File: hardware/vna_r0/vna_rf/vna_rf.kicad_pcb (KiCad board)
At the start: 4 copper layers, 78 x 49 mm, 258 parts, among them J301 RF_Shield_Two_Pieces, J302 RF_Shield_Two_Pieces, J401 CONN_02X10, J402 RF_Shield_Two_Pieces, U201 LMX2594, U202 LTC2630, U203 ADRF5040, U204 LTC2054CS5, U205 MAAM-011100, U301 NC7WZU04, U302 PE42521, U303 MASW-008322-TR1000, U304 PE42521, U401 CONN_SMA_2GND, U402 CONN_SMA_2GND, U403 CONN_SMA, U404 CONN_SMA, U405 CONN_SMA, U406 CONN_SMA_2GND

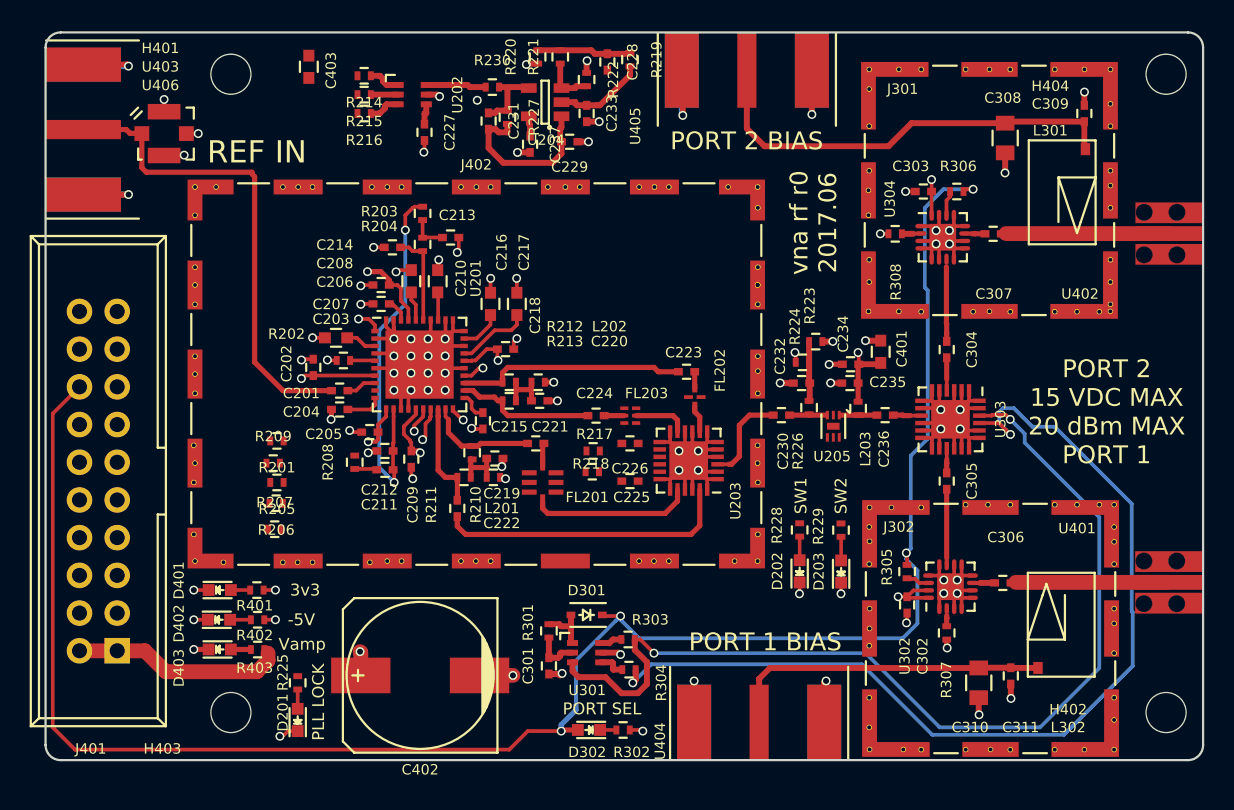
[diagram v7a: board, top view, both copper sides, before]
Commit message: finished vna rf r0 layout
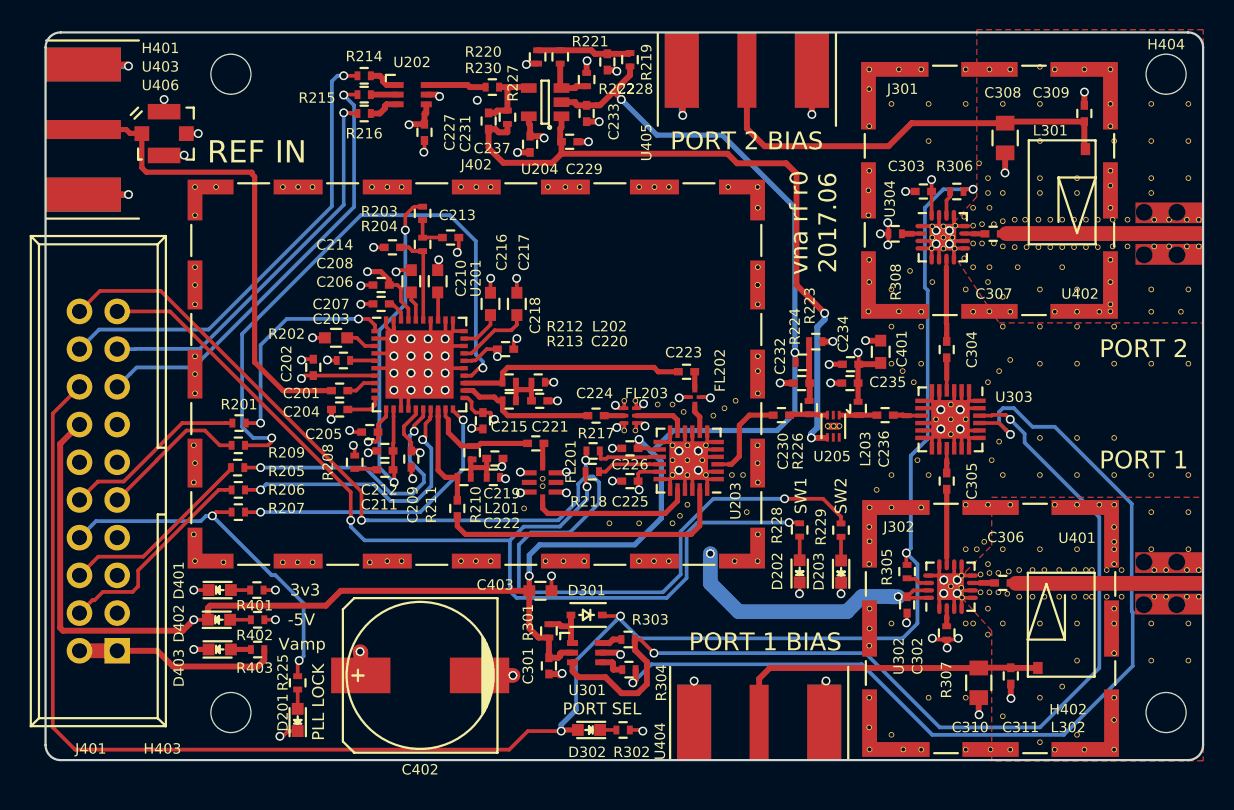
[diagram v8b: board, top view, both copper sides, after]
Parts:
- added REF**: VIA_OSH4LAYER_MIN, vna_footprints:VIA_OSH4LAYER_MIN, F.Cu at (207.8, 107.2)
- added REF**: VIA_OSH4LAYER_MIN, vna_footprints:VIA_OSH4LAYER_MIN, F.Cu at (216.8, 100.2)
- added REF**: VIA_OSH4LAYER_MIN, vna_footprints:VIA_OSH4LAYER_MIN, F.Cu at (252.0, 94.0)
- added REF**: VIA_OSH4LAYER_MIN, vna_footprints:VIA_OSH4LAYER_MIN, F.Cu at (250.0, 94.0)
- added REF**: VIA_OSH4LAYER_MIN, vna_footprints:VIA_OSH4LAYER_MIN, F.Cu at (244.0, 91.0)
- added REF**: VIA_OSH4LAYER_MIN, vna_footprints:VIA_OSH4LAYER_MIN, F.Cu at (241.0, 91.0)
- added REF**: VIA_OSH4LAYER_MIN, vna_footprints:VIA_OSH4LAYER_MIN, F.Cu at (240.0, 121.2)
- added REF**: VIA_OSH4LAYER_MIN, vna_footprints:VIA_OSH4LAYER_MIN, F.Cu at (242.5, 123.0)
- added REF**: VIA_OSH4LAYER_MIN, vna_footprints:VIA_OSH4LAYER_MIN, F.Cu at (245.0, 122.5)
- added REF**: VIA_OSH4LAYER_MIN, vna_footprints:VIA_OSH4LAYER_MIN, F.Cu at (242.5, 120.0)
- added REF**: VIA_OSH4LAYER_MIN, vna_footprints:VIA_OSH4LAYER_MIN, F.Cu at (244.0, 119.2)
- added REF**: VIA_OSH4LAYER_MIN, vna_footprints:VIA_OSH4LAYER_MIN, F.Cu at (245.0, 117.5)
- added REF**: VIA_OSH4LAYER_MIN, vna_footprints:VIA_OSH4LAYER_MIN, F.Cu at (217.8, 100.2)
- added REF**: VIA_OSH4LAYER_MIN, vna_footprints:VIA_OSH4LAYER_MIN, F.Cu at (250.0, 117.5)
- added REF**: VIA_OSH4LAYER_MIN, vna_footprints:VIA_OSH4LAYER_MIN, F.Cu at (252.5, 117.5)
- added REF**: VIA_OSH4LAYER_MIN, vna_footprints:VIA_OSH4LAYER_MIN, F.Cu at (252.5, 115.0)
- added REF**: VIA_OSH4LAYER_MIN, vna_footprints:VIA_OSH4LAYER_MIN, F.Cu at (250.0, 115.0)
- added REF**: VIA_OSH4LAYER_MIN, vna_footprints:VIA_OSH4LAYER_MIN, F.Cu at (245.0, 115.0)
- added REF**: VIA_OSH4LAYER_MIN, vna_footprints:VIA_OSH4LAYER_MIN, F.Cu at (242.5, 115.0)
- added REF**: VIA_OSH4LAYER_MIN, vna_footprints:VIA_OSH4LAYER_MIN, F.Cu at (240.0, 115.0)
- added REF**: VIA_OSH4LAYER_MIN, vna_footprints:VIA_OSH4LAYER_MIN, F.Cu at (240.0, 110.0)
- added REF**: VIA_OSH4LAYER_MIN, vna_footprints:VIA_OSH4LAYER_MIN, F.Cu at (242.5, 110.0)
- added REF**: VIA_OSH4LAYER_MIN, vna_footprints:VIA_OSH4LAYER_MIN, F.Cu at (245.0, 110.0)
- added REF**: VIA_OSH4LAYER_MIN, vna_footprints:VIA_OSH4LAYER_MIN, F.Cu at (218.5, 100.8)
- added REF**: VIA_OSH4LAYER_MIN, vna_footprints:VIA_OSH4LAYER_MIN, F.Cu at (247.5, 110.0)
- added REF**: VIA_OSH4LAYER_MIN, vna_footprints:VIA_OSH4LAYER_MIN, F.Cu at (250.0, 110.0)
- added REF**: VIA_OSH4LAYER_MIN, vna_footprints:VIA_OSH4LAYER_MIN, F.Cu at (252.5, 110.0)
- added REF**: VIA_OSH4LAYER_MIN, vna_footprints:VIA_OSH4LAYER_MIN, F.Cu at (250.0, 107.5)
- added REF**: VIA_OSH4LAYER_MIN, vna_footprints:VIA_OSH4LAYER_MIN, F.Cu at (252.5, 107.5)
- added REF**: VIA_OSH4LAYER_MIN, vna_footprints:VIA_OSH4LAYER_MIN, F.Cu at (242.5, 92.5)
- added REF**: VIA_OSH4LAYER_MIN, vna_footprints:VIA_OSH4LAYER_MIN, F.Cu at (245.0, 92.5)
- added REF**: VIA_OSH4LAYER_MIN, vna_footprints:VIA_OSH4LAYER_MIN, F.Cu at (250.0, 92.5)
- added REF**: VIA_OSH4LAYER_MIN, vna_footprints:VIA_OSH4LAYER_MIN, F.Cu at (252.5, 92.5)
- added REF**: VIA_OSH4LAYER_MIN, vna_footprints:VIA_OSH4LAYER_MIN, F.Cu at (252.5, 85.0)
- added REF**: VIA_OSH4LAYER_MIN, vna_footprints:VIA_OSH4LAYER_MIN, F.Cu at (217.8, 108.2)
- added REF**: VIA_OSH4LAYER_MIN, vna_footprints:VIA_OSH4LAYER_MIN, F.Cu at (250.0, 85.0)
- added REF**: VIA_OSH4LAYER_MIN, vna_footprints:VIA_OSH4LAYER_MIN, F.Cu at (245.0, 85.0)
- added REF**: VIA_OSH4LAYER_MIN, vna_footprints:VIA_OSH4LAYER_MIN, F.Cu at (242.5, 85.0)
- added REF**: VIA_OSH4LAYER_MIN, vna_footprints:VIA_OSH4LAYER_MIN, F.Cu at (242.5, 77.5)
- added REF**: VIA_OSH4LAYER_MIN, vna_footprints:VIA_OSH4LAYER_MIN, F.Cu at (252.5, 80.0)
- added REF**: VIA_OSH4LAYER_MIN, vna_footprints:VIA_OSH4LAYER_MIN, F.Cu at (250.0, 80.0)
- added REF**: VIA_OSH4LAYER_MIN, vna_footprints:VIA_OSH4LAYER_MIN, F.Cu at (240.0, 80.0)
- added REF**: VIA_OSH4LAYER_MIN, vna_footprints:VIA_OSH4LAYER_MIN, F.Cu at (242.5, 80.0)
- added REF**: VIA_OSH4LAYER_MIN, vna_footprints:VIA_OSH4LAYER_MIN, F.Cu at (247.5, 82.5)
- added REF**: VIA_OSH4LAYER_MIN, vna_footprints:VIA_OSH4LAYER_MIN, F.Cu at (252.5, 82.5)
- added REF**: VIA_OSH4LAYER_MIN, vna_footprints:VIA_OSH4LAYER_MIN, F.Cu at (218.2, 107.8)
- added REF**: VIA_OSH4LAYER_MIN, vna_footprints:VIA_OSH4LAYER_MIN, F.Cu at (242.5, 82.5)
- added REF**: VIA_OSH4LAYER_MIN, vna_footprints:VIA_OSH4LAYER_MIN, F.Cu at (250.0, 82.5)
- added REF**: VIA_OSH4LAYER_MIN, vna_footprints:VIA_OSH4LAYER_MIN, F.Cu at (250.0, 86.0)
- added REF**: VIA_OSH4LAYER_MIN, vna_footprints:VIA_OSH4LAYER_MIN, F.Cu at (245.0, 86.0)
- added REF**: VIA_OSH4LAYER_MIN, vna_footprints:VIA_OSH4LAYER_MIN, F.Cu at (242.5, 86.0)
- added REF**: VIA_OSH4LAYER_MIN, vna_footprints:VIA_OSH4LAYER_MIN, F.Cu at (240.0, 86.0)
- added REF**: VIA_OSH4LAYER_MIN, vna_footprints:VIA_OSH4LAYER_MIN, F.Cu at (239.0, 85.0)
- added REF**: VIA_OSH4LAYER_MIN, vna_footprints:VIA_OSH4LAYER_MIN, F.Cu at (239.0, 86.0)
- added REF**: VIA_OSH4LAYER_MIN, vna_footprints:VIA_OSH4LAYER_MIN, F.Cu at (238.0, 87.0)
- added REF**: VIA_OSH4LAYER_MIN, vna_footprints:VIA_OSH4LAYER_MIN, F.Cu at (240.0, 93.0)
- added REF**: VIA_OSH4LAYER_MIN, vna_footprints:VIA_OSH4LAYER_MIN, F.Cu at (218.8, 107.0)
- added REF**: VIA_OSH4LAYER_MIN, vna_footprints:VIA_OSH4LAYER_MIN, F.Cu at (239.0, 92.0)
- added REF**: VIA_OSH4LAYER_MIN, vna_footprints:VIA_OSH4LAYER_MIN, F.Cu at (238.0, 91.0)
- added REF**: VIA_OSH4LAYER_MIN, vna_footprints:VIA_OSH4LAYER_MIN, F.Cu at (237.4, 87.6)
- added REF**: VIA_OSH4LAYER_MIN, vna_footprints:VIA_OSH4LAYER_MIN, F.Cu at (237.4, 90.4)
- added REF**: VIA_OSH4LAYER_MIN, vna_footprints:VIA_OSH4LAYER_MIN, F.Cu at (253.2, 87.8)
- added REF**: VIA_OSH4LAYER_MIN, vna_footprints:VIA_OSH4LAYER_MIN, F.Cu at (253.2, 89.6)
- added REF**: VIA_OSH4LAYER_MIN, vna_footprints:VIA_OSH4LAYER_MIN, F.Cu at (252.4, 89.6)
- added REF**: VIA_OSH4LAYER_MIN, vna_footprints:VIA_OSH4LAYER_MIN, F.Cu at (252.4, 87.8)
- added REF**: VIA_OSH4LAYER_MIN, vna_footprints:VIA_OSH4LAYER_MIN, F.Cu at (251.2, 87.8)
- added REF**: VIA_OSH4LAYER_MIN, vna_footprints:VIA_OSH4LAYER_MIN, F.Cu at (251.2, 89.6)
- added REF**: VIA_OSH4LAYER_MIN, vna_footprints:VIA_OSH4LAYER_MIN, F.Cu at (209.0, 105.8)
- added REF**: VIA_OSH4LAYER_MIN, vna_footprints:VIA_OSH4LAYER_MIN, F.Cu at (250.2, 89.6)
- added REF**: VIA_OSH4LAYER_MIN, vna_footprints:VIA_OSH4LAYER_MIN, F.Cu at (250.2, 87.8)
- added REF**: VIA_OSH4LAYER_MIN, vna_footprints:VIA_OSH4LAYER_MIN, F.Cu at (248.4, 87.8)
- added REF**: VIA_OSH4LAYER_MIN, vna_footprints:VIA_OSH4LAYER_MIN, F.Cu at (248.4, 89.6)
- added REF**: VIA_OSH4LAYER_MIN, vna_footprints:VIA_OSH4LAYER_MIN, F.Cu at (247.4, 89.6)
- added REF**: VIA_OSH4LAYER_MIN, vna_footprints:VIA_OSH4LAYER_MIN, F.Cu at (247.4, 87.8)
- added REF**: VIA_OSH4LAYER_MIN, vna_footprints:VIA_OSH4LAYER_MIN, F.Cu at (246.4, 87.8)
- added REF**: VIA_OSH4LAYER_MIN, vna_footprints:VIA_OSH4LAYER_MIN, F.Cu at (245.6, 87.8)
- added REF**: VIA_OSH4LAYER_MIN, vna_footprints:VIA_OSH4LAYER_MIN, F.Cu at (244.8, 87.8)
- added REF**: VIA_OSH4LAYER_MIN, vna_footprints:VIA_OSH4LAYER_MIN, F.Cu at (244.0, 87.8)
- added REF**: VIA_OSH4LAYER_MIN, vna_footprints:VIA_OSH4LAYER_MIN, F.Cu at (209.0, 105.2)
- added REF**: VIA_OSH4LAYER_MIN, vna_footprints:VIA_OSH4LAYER_MIN, F.Cu at (246.4, 89.7)
- added REF**: VIA_OSH4LAYER_MIN, vna_footprints:VIA_OSH4LAYER_MIN, F.Cu at (245.6, 89.7)
- added REF**: VIA_OSH4LAYER_MIN, vna_footprints:VIA_OSH4LAYER_MIN, F.Cu at (244.8, 89.7)
- added REF**: VIA_OSH4LAYER_MIN, vna_footprints:VIA_OSH4LAYER_MIN, F.Cu at (244.0, 89.7)
- added REF**: VIA_OSH4LAYER_MIN, vna_footprints:VIA_OSH4LAYER_MIN, F.Cu at (243.2, 89.7)
- added REF**: VIA_OSH4LAYER_MIN, vna_footprints:VIA_OSH4LAYER_MIN, F.Cu at (243.2, 87.8)
- added REF**: VIA_OSH4LAYER_MIN, vna_footprints:VIA_OSH4LAYER_MIN, F.Cu at (242.4, 87.8)
- added REF**: VIA_OSH4LAYER_MIN, vna_footprints:VIA_OSH4LAYER_MIN, F.Cu at (242.4, 89.7)
- added REF**: VIA_OSH4LAYER_MIN, vna_footprints:VIA_OSH4LAYER_MIN, F.Cu at (241.5, 87.8)
- added REF**: VIA_OSH4LAYER_MIN, vna_footprints:VIA_OSH4LAYER_MIN, F.Cu at (241.6, 89.7)
- added REF**: VIA_OSH4LAYER_MIN, vna_footprints:VIA_OSH4LAYER_MIN, F.Cu at (215.2, 102.0)
- added REF**: VIA_OSH4LAYER_MIN, vna_footprints:VIA_OSH4LAYER_MIN, F.Cu at (240.8, 89.7)
- added REF**: VIA_OSH4LAYER_MIN, vna_footprints:VIA_OSH4LAYER_MIN, F.Cu at (240.8, 87.8)
- added REF**: VIA_OSH4LAYER_MIN, vna_footprints:VIA_OSH4LAYER_MIN, F.Cu at (240.0, 87.9)
- added REF**: VIA_OSH4LAYER_MIN, vna_footprints:VIA_OSH4LAYER_MIN, F.Cu at (240.0, 89.6)
- added REF**: VIA_OSH4LAYER_MIN, vna_footprints:VIA_OSH4LAYER_MIN, F.Cu at (239.4, 89.4)
- added REF**: VIA_OSH4LAYER_MIN, vna_footprints:VIA_OSH4LAYER_MIN, F.Cu at (239.4, 88.1)
- added REF**: VIA_OSH4LAYER_MIN, vna_footprints:VIA_OSH4LAYER_MIN, F.Cu at (238.6, 88.1)
- added REF**: VIA_OSH4LAYER_MIN, vna_footprints:VIA_OSH4LAYER_MIN, F.Cu at (238.4, 84.0)
- added REF**: VIA_OSH4LAYER_MIN, vna_footprints:VIA_OSH4LAYER_MIN, F.Cu at (238.6, 89.4)
- added REF**: VIA_OSH4LAYER_MIN, vna_footprints:VIA_OSH4LAYER_MIN, F.Cu at (238.0, 89.4)
- added REF**: VIA_OSH4LAYER_MIN, vna_footprints:VIA_OSH4LAYER_MIN, F.Cu at (214.5, 102.0)
- added REF**: VIA_OSH4LAYER_MIN, vna_footprints:VIA_OSH4LAYER_MIN, F.Cu at (238.0, 88.2)
- added REF**: VIA_OSH4LAYER_MIN, vna_footprints:VIA_OSH4LAYER_MIN, F.Cu at (237.2, 111.8)
- added REF**: VIA_OSH4LAYER_MIN, vna_footprints:VIA_OSH4LAYER_MIN, F.Cu at (237.2, 112.6)
- added REF**: VIA_OSH4LAYER_MIN, vna_footprints:VIA_OSH4LAYER_MIN, F.Cu at (236.8, 88.2)
- added REF**: VIA_OSH4LAYER_MIN, vna_footprints:VIA_OSH4LAYER_MIN, F.Cu at (236.6, 89.0)
- added REF**: VIA_OSH4LAYER_MIN, vna_footprints:VIA_OSH4LAYER_MIN, F.Cu at (253.2, 113.2)
- added REF**: VIA_OSH4LAYER_MIN, vna_footprints:VIA_OSH4LAYER_MIN, F.Cu at (253.2, 111.4)
- added REF**: VIA_OSH4LAYER_MIN, vna_footprints:VIA_OSH4LAYER_MIN, F.Cu at (252.4, 111.4)
- added REF**: VIA_OSH4LAYER_MIN, vna_footprints:VIA_OSH4LAYER_MIN, F.Cu at (252.4, 113.2)
- added REF**: VIA_OSH4LAYER_MIN, vna_footprints:VIA_OSH4LAYER_MIN, F.Cu at (251.0, 113.2)
- added REF**: VIA_OSH4LAYER_MIN, vna_footprints:VIA_OSH4LAYER_MIN, F.Cu at (213.5, 108.2)
- added REF**: VIA_OSH4LAYER_MIN, vna_footprints:VIA_OSH4LAYER_MIN, F.Cu at (214.5, 100.0)
- added REF**: VIA_OSH4LAYER_MIN, vna_footprints:VIA_OSH4LAYER_MIN, F.Cu at (251.0, 111.4)
- added REF**: VIA_OSH4LAYER_MIN, vna_footprints:VIA_OSH4LAYER_MIN, F.Cu at (250.2, 111.4)
- added REF**: VIA_OSH4LAYER_MIN, vna_footprints:VIA_OSH4LAYER_MIN, F.Cu at (250.2, 113.2)
- added REF**: VIA_OSH4LAYER_MIN, vna_footprints:VIA_OSH4LAYER_MIN, F.Cu at (248.0, 111.4)
- added REF**: VIA_OSH4LAYER_MIN, vna_footprints:VIA_OSH4LAYER_MIN, F.Cu at (248.0, 113.2)
- added REF**: VIA_OSH4LAYER_MIN, vna_footprints:VIA_OSH4LAYER_MIN, F.Cu at (247.0, 113.2)
- added REF**: VIA_OSH4LAYER_MIN, vna_footprints:VIA_OSH4LAYER_MIN, F.Cu at (247.0, 111.4)
- added REF**: VIA_OSH4LAYER_MIN, vna_footprints:VIA_OSH4LAYER_MIN, F.Cu at (246.0, 111.4)
- added REF**: VIA_OSH4LAYER_MIN, vna_footprints:VIA_OSH4LAYER_MIN, F.Cu at (246.0, 113.2)
- added REF**: VIA_OSH4LAYER_MIN, vna_footprints:VIA_OSH4LAYER_MIN, F.Cu at (245.6, 113.2)
- added REF**: VIA_OSH4LAYER_MIN, vna_footprints:VIA_OSH4LAYER_MIN, F.Cu at (215.2, 100.0)
- added REF**: VIA_OSH4LAYER_MIN, vna_footprints:VIA_OSH4LAYER_MIN, F.Cu at (245.6, 111.4)
- added REF**: VIA_OSH4LAYER_MIN, vna_footprints:VIA_OSH4LAYER_MIN, F.Cu at (244.8, 111.4)
- added REF**: VIA_OSH4LAYER_MIN, vna_footprints:VIA_OSH4LAYER_MIN, F.Cu at (244.8, 113.2)
- added REF**: VIA_OSH4LAYER_MIN, vna_footprints:VIA_OSH4LAYER_MIN, F.Cu at (243.8, 113.2)
- added REF**: VIA_OSH4LAYER_MIN, vna_footprints:VIA_OSH4LAYER_MIN, F.Cu at (243.8, 111.4)
- added REF**: VIA_OSH4LAYER_MIN, vna_footprints:VIA_OSH4LAYER_MIN, F.Cu at (242.8, 111.4)
- added REF**: VIA_OSH4LAYER_MIN, vna_footprints:VIA_OSH4LAYER_MIN, F.Cu at (242.8, 113.2)
- added REF**: VIA_OSH4LAYER_MIN, vna_footprints:VIA_OSH4LAYER_MIN, F.Cu at (242.0, 113.2)
- added REF**: VIA_OSH4LAYER_MIN, vna_footprints:VIA_OSH4LAYER_MIN, F.Cu at (242.0, 111.4)
- added REF**: VIA_OSH4LAYER_MIN, vna_footprints:VIA_OSH4LAYER_MIN, F.Cu at (241.1, 113.2)
- added REF**: VIA_OSH4LAYER_MIN, vna_footprints:VIA_OSH4LAYER_MIN, F.Cu at (233.8, 91.2)
- added REF**: VIA_OSH4LAYER_MIN, vna_footprints:VIA_OSH4LAYER_MIN, F.Cu at (241.1, 111.4)
- added REF**: VIA_OSH4LAYER_MIN, vna_footprints:VIA_OSH4LAYER_MIN, F.Cu at (240.4, 111.5)
- added REF**: VIA_OSH4LAYER_MIN, vna_footprints:VIA_OSH4LAYER_MIN, F.Cu at (240.3, 113.0)
- added REF**: VIA_OSH4LAYER_MIN, vna_footprints:VIA_OSH4LAYER_MIN, F.Cu at (239.7, 112.9)
- added REF**: VIA_OSH4LAYER_MIN, vna_footprints:VIA_OSH4LAYER_MIN, F.Cu at (239.7, 111.6)
- added REF**: VIA_OSH4LAYER_MIN, vna_footprints:VIA_OSH4LAYER_MIN, F.Cu at (239.1, 111.6)
- added REF**: VIA_OSH4LAYER_MIN, vna_footprints:VIA_OSH4LAYER_MIN, F.Cu at (239.1, 112.9)
- added REF**: VIA_OSH4LAYER_MIN, vna_footprints:VIA_OSH4LAYER_MIN, F.Cu at (238.5, 112.9)
- added REF**: VIA_OSH4LAYER_MIN, vna_footprints:VIA_OSH4LAYER_MIN, F.Cu at (238.5, 111.7)
- added REF**: VIA_OSH4LAYER_MIN, vna_footprints:VIA_OSH4LAYER_MIN, F.Cu at (228.2, 101.7)
- added REF**: VIA_OSH4LAYER_MIN, vna_footprints:VIA_OSH4LAYER_MIN, F.Cu at (239.0, 115.8)
- added REF**: VIA_OSH4LAYER_MIN, vna_footprints:VIA_OSH4LAYER_MIN, F.Cu at (228.6, 101.7)
- added REF**: VIA_OSH4LAYER_MIN, vna_footprints:VIA_OSH4LAYER_MIN, F.Cu at (229.0, 101.7)
- added REF**: VIA_OSH4LAYER_MIN, vna_footprints:VIA_OSH4LAYER_MIN, F.Cu at (211.8, 110.8)
- added REF**: VIA_OSH4LAYER_MIN, vna_footprints:VIA_OSH4LAYER_MIN, F.Cu at (210.4, 110.8)
- added REF**: VIA_OSH4LAYER_MIN, vna_footprints:VIA_OSH4LAYER_MIN, F.Cu at (209.2, 110.8)
- added REF**: VIA_OSH4LAYER_MIN, vna_footprints:VIA_OSH4LAYER_MIN, F.Cu at (238.0, 115.0)
- added REF**: VIA_OSH4LAYER_MIN, vna_footprints:VIA_OSH4LAYER_MIN, F.Cu at (238.8, 109.5)
- added REF**: VIA_OSH4LAYER_MIN, vna_footprints:VIA_OSH4LAYER_MIN, F.Cu at (238.2, 110.0)
- added REF**: VIA_OSH4LAYER_MIN, vna_footprints:VIA_OSH4LAYER_MIN, F.Cu at (231.5, 106.0)
- added REF**: VIA_OSH4LAYER_MIN, vna_footprints:VIA_OSH4LAYER_MIN, F.Cu at (239.8, 98.0)
- added REF**: VIA_OSH4LAYER_MIN, vna_footprints:VIA_OSH4LAYER_MIN, F.Cu at (233.2, 98.0)
- added REF**: VIA_OSH4LAYER_MIN, vna_footprints:VIA_OSH4LAYER_MIN, F.Cu at (215.5, 108.2)
- added REF**: VIA_OSH4LAYER_MIN, vna_footprints:VIA_OSH4LAYER_MIN, F.Cu at (239.0, 98.8)
- added REF**: VIA_OSH4LAYER_MIN, vna_footprints:VIA_OSH4LAYER_MIN, F.Cu at (234.0, 98.8)
- added REF**: VIA_OSH4LAYER_MIN, vna_footprints:VIA_OSH4LAYER_MIN, F.Cu at (234.2, 104.0)
- added REF**: VIA_OSH4LAYER_MIN, vna_footprints:VIA_OSH4LAYER_MIN, F.Cu at (239.2, 104.0)
- added REF**: VIA_OSH4LAYER_MIN, vna_footprints:VIA_OSH4LAYER_MIN, F.Cu at (235.2, 88.2)
- added REF**: VIA_OSH4LAYER_MIN, vna_footprints:VIA_OSH4LAYER_MIN, F.Cu at (235.2, 89.7)
- added REF**: VIA_OSH4LAYER_MIN, vna_footprints:VIA_OSH4LAYER_MIN, F.Cu at (236.8, 89.8)
- added REF**: VIA_OSH4LAYER_MIN, vna_footprints:VIA_OSH4LAYER_MIN, F.Cu at (236.0, 89.8)
- added REF**: VIA_OSH4LAYER_MIN, vna_footprints:VIA_OSH4LAYER_MIN, F.Cu at (236.0, 88.2)
- added REF**: VIA_OSH4LAYER_MIN, vna_footprints:VIA_OSH4LAYER_MIN, F.Cu at (235.2, 89.0)
- added REF**: VIA_OSH4LAYER_MIN, vna_footprints:VIA_OSH4LAYER_MIN, F.Cu at (222.5, 105.0)
- added REF**: VIA_OSH4LAYER_MIN, vna_footprints:VIA_OSH4LAYER_MIN, F.Cu at (236.0, 89.0)
- added REF**: VIA_OSH4LAYER_MIN, vna_footprints:VIA_OSH4LAYER_MIN, F.Cu at (235.5, 101.2)
- added REF**: VIA_OSH4LAYER_MIN, vna_footprints:VIA_OSH4LAYER_MIN, F.Cu at (237.5, 101.2)
- added REF**: VIA_OSH4LAYER_MIN, vna_footprints:VIA_OSH4LAYER_MIN, F.Cu at (236.5, 102.2)
- added REF**: VIA_OSH4LAYER_MIN, vna_footprints:VIA_OSH4LAYER_MIN, F.Cu at (236.5, 100.2)
- added REF**: VIA_OSH4LAYER_MIN, vna_footprints:VIA_OSH4LAYER_MIN, F.Cu at (236.5, 101.2)
- added REF**: VIA_OSH4LAYER_MIN, vna_footprints:VIA_OSH4LAYER_MIN, F.Cu at (237.2, 113.2)
- added REF**: VIA_OSH4LAYER_MIN, vna_footprints:VIA_OSH4LAYER_MIN, F.Cu at (236.5, 112.5)
- added REF**: VIA_OSH4LAYER_MIN, vna_footprints:VIA_OSH4LAYER_MIN, F.Cu at (217.8, 105.0)
- added REF**: VIA_OSH4LAYER_MIN, vna_footprints:VIA_OSH4LAYER_MIN, F.Cu at (219.8, 104.0)
- added REF**: VIA_OSH4LAYER_MIN, vna_footprints:VIA_OSH4LAYER_MIN, F.Cu at (221.8, 105.0)
- added REF**: VIA_OSH4LAYER_MIN, vna_footprints:VIA_OSH4LAYER_MIN, F.Cu at (220.0, 105.0)
- added REF**: VIA_OSH4LAYER_MIN, vna_footprints:VIA_OSH4LAYER_MIN, F.Cu at (220.0, 103.0)
- added REF**: VIA_OSH4LAYER_MIN, vna_footprints:VIA_OSH4LAYER_MIN, F.Cu at (218.8, 103.0)
- added REF**: VIA_OSH4LAYER_MIN, vna_footprints:VIA_OSH4LAYER_MIN, F.Cu at (218.8, 105.0)
- added REF**: VIA_OSH4LAYER_MIN, vna_footprints:VIA_OSH4LAYER_MIN, F.Cu at (217.8, 104.0)
- added REF**: VIA_OSH4LAYER_MIN, vna_footprints:VIA_OSH4LAYER_MIN, F.Cu at (217.8, 103.0)
- added REF**: VIA_OSH4LAYER_MIN, vna_footprints:VIA_OSH4LAYER_MIN, F.Cu at (218.8, 104.0)
- added REF**: VIA_OSH4LAYER_MIN, vna_footprints:VIA_OSH4LAYER_MIN, F.Cu at (232.5, 122.5)
- added REF**: VIA_OSH4LAYER_MIN, vna_footprints:VIA_OSH4LAYER_MIN, F.Cu at (235.0, 120.0)
- added REF**: VIA_OSH4LAYER_MIN, vna_footprints:VIA_OSH4LAYER_MIN, F.Cu at (237.5, 120.0)
- added REF**: VIA_OSH4LAYER_MIN, vna_footprints:VIA_OSH4LAYER_MIN, F.Cu at (222.8, 107.5)
- added REF**: VIA_OSH4LAYER_MIN, vna_footprints:VIA_OSH4LAYER_MIN, F.Cu at (237.5, 115.0)
- added REF**: VIA_OSH4LAYER_MIN, vna_footprints:VIA_OSH4LAYER_MIN, F.Cu at (232.5, 115.0)
- added REF**: VIA_OSH4LAYER_MIN, vna_footprints:VIA_OSH4LAYER_MIN, F.Cu at (237.5, 110.0)
- added REF**: VIA_OSH4LAYER_MIN, vna_footprints:VIA_OSH4LAYER_MIN, F.Cu at (237.5, 92.5)
- added REF**: VIA_OSH4LAYER_MIN, vna_footprints:VIA_OSH4LAYER_MIN, F.Cu at (237.5, 80.0)
- added REF**: VIA_OSH4LAYER_MIN, vna_footprints:VIA_OSH4LAYER_MIN, F.Cu at (235.0, 80.0)
- added REF**: VIA_OSH4LAYER_MIN, vna_footprints:VIA_OSH4LAYER_MIN, F.Cu at (232.5, 80.0)
- added REF**: VIA_OSH4LAYER_MIN, vna_footprints:VIA_OSH4LAYER_MIN, F.Cu at (235.0, 82.5)
- added REF**: VIA_OSH4LAYER_MIN, vna_footprints:VIA_OSH4LAYER_MIN, F.Cu at (232.5, 92.5)
- added REF**: VIA_OSH4LAYER_MIN, vna_footprints:VIA_OSH4LAYER_MIN, F.Cu at (235.2, 92.0)
- added REF**: VIA_OSH4LAYER_MIN, vna_footprints:VIA_OSH4LAYER_MIN, F.Cu at (222.0, 100.0)
- added REF**: VIA_OSH4LAYER_MIN, vna_footprints:VIA_OSH4LAYER_MIN, F.Cu at (234.5, 95.0)
- added REF**: VIA_OSH4LAYER_MIN, vna_footprints:VIA_OSH4LAYER_MIN, F.Cu at (232.5, 95.0)
- added REF**: VIA_OSH4LAYER_MIN, vna_footprints:VIA_OSH4LAYER_MIN, F.Cu at (232.5, 97.5)
- added REF**: VIA_OSH4LAYER_MIN, vna_footprints:VIA_OSH4LAYER_MIN, F.Cu at (232.5, 105.0)
- added REF**: VIA_OSH4LAYER_MIN, vna_footprints:VIA_OSH4LAYER_MIN, F.Cu at (235.0, 105.0)
- added REF**: VIA_OSH4LAYER_MIN, vna_footprints:VIA_OSH4LAYER_MIN, F.Cu at (234.5, 97.5)
- added REF**: VIA_OSH4LAYER_MIN, vna_footprints:VIA_OSH4LAYER_MIN, F.Cu at (239.8, 102.8)
- added REF**: VIA_OSH4LAYER_MIN, vna_footprints:VIA_OSH4LAYER_MIN, F.Cu at (242.5, 102.5)
- added REF**: VIA_OSH4LAYER_MIN, vna_footprints:VIA_OSH4LAYER_MIN, F.Cu at (245.0, 102.5)
- added REF**: VIA_OSH4LAYER_MIN, vna_footprints:VIA_OSH4LAYER_MIN, F.Cu at (247.5, 102.5)
- added REF**: VIA_OSH4LAYER_MIN, vna_footprints:VIA_OSH4LAYER_MIN, F.Cu at (221.2, 100.5)
- added REF**: VIA_OSH4LAYER_MIN, vna_footprints:VIA_OSH4LAYER_MIN, F.Cu at (247.5, 95.0)
- added REF**: VIA_OSH4LAYER_MIN, vna_footprints:VIA_OSH4LAYER_MIN, F.Cu at (245.0, 95.0)
- added REF**: VIA_OSH4LAYER_MIN, vna_footprints:VIA_OSH4LAYER_MIN, F.Cu at (242.5, 95.0)
- added REF**: VIA_OSH4LAYER_MIN, vna_footprints:VIA_OSH4LAYER_MIN, F.Cu at (240.0, 95.0)
- added REF**: VIA_OSH4LAYER_MIN, vna_footprints:VIA_OSH4LAYER_MIN, F.Cu at (245.0, 97.5)
- added REF**: VIA_OSH4LAYER_MIN, vna_footprints:VIA_OSH4LAYER_MIN, F.Cu at (247.5, 97.5)
- added REF**: VIA_OSH4LAYER_MIN, vna_footprints:VIA_OSH4LAYER_MIN, F.Cu at (250.0, 97.5)
- added REF**: VIA_OSH4LAYER_MIN, vna_footprints:VIA_OSH4LAYER_MIN, F.Cu at (252.5, 105.0)
- added REF**: VIA_OSH4LAYER_MIN, vna_footprints:VIA_OSH4LAYER_MIN, F.Cu at (250.0, 105.0)
- added REF**: VIA_OSH4LAYER_MIN, vna_footprints:VIA_OSH4LAYER_MIN, F.Cu at (247.5, 105.0)
- added REF**: VIA_OSH4LAYER_MIN, vna_footprints:VIA_OSH4LAYER_MIN, F.Cu at (220.5, 101.0)
- added REF**: VIA_OSH4LAYER_MIN, vna_footprints:VIA_OSH4LAYER_MIN, F.Cu at (245.0, 105.0)
- added REF**: VIA_OSH4LAYER_MIN, vna_footprints:VIA_OSH4LAYER_MIN, F.Cu at (242.5, 105.0)
- added REF**: VIA_OSH4LAYER_MIN, vna_footprints:VIA_OSH4LAYER_MIN, F.Cu at (240.0, 105.0)
- added REF**: VIA_OSH4LAYER_MIN, vna_footprints:VIA_OSH4LAYER_MIN, F.Cu at (242.5, 97.5)
- added REF**: VIA_OSH4LAYER_MIN, vna_footprints:VIA_OSH4LAYER_MIN, F.Cu at (240.5, 97.2)
- added REF**: VIA_OSH4LAYER_MIN, vna_footprints:VIA_OSH4LAYER_MIN, F.Cu at (252.5, 97.5)
- added REF**: VIA_OSH4LAYER_MIN, vna_footprints:VIA_OSH4LAYER_MIN, F.Cu at (239.0, 114.0)
- added REF**: VIA_OSH4LAYER_MIN, vna_footprints:VIA_OSH4LAYER_MIN, F.Cu at (239.0, 111.0)
- added REF**: VIA_OSH4LAYER_MIN, vna_footprints:VIA_OSH4LAYER_MIN, F.Cu at (239.1, 87.0)
- added REF**: VIA_OSH4LAYER_MIN, vna_footprints:VIA_OSH4LAYER_MIN, F.Cu at (239.1, 91.0)
- moved C403 38.6 mm to (208.8, 112.8), turned to 180 degrees
- moved R205 2.83 mm to (188.4, 104.5)
- moved R201 2.82 mm to (188.6, 101.5)
- moved R207 2.71 mm to (188.5, 107.5), turned to 180 degrees
- moved R206 2.70 mm to (188.5, 106.0)
- moved R209 2.64 mm to (188.5, 103.0)
- moved C226 0.33 mm to (214.9, 103.2)
- moved U401 0.07 mm to (251.2, 112.3)
- turned R217 to 180 degrees
- turned R218 to 180 degrees
- turned R229 to 270 degrees
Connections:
- R228 pad 2: /rf_synth/RFSW_V1 -> /RFSW_1
- R229 pad 1: Net-(D203-Pad2) -> /RFSW_2
- R229 pad 2: /rf_synth/RFSW_V2 -> Net-(D203-Pad2)
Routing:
- net -5V: track 11.0 -> 122.1 mm, vias 2 -> 5
- net /RFSW_2: track 0.00 -> 84.9 mm, vias 0 -> 3
- net /AMP_5V: track 19.3 -> 91.2 mm
- net /RFSW_1: track 0.00 -> 69.5 mm, vias 0 -> 3
- net Net-(R209-Pad2): track 1.48 -> 40.7 mm, vias 1 -> 2
- net /rf_synth/AMP_VC: track 11.2 -> 47.5 mm, vias 0 -> 2
- net +3V3: track 35.0 -> 70.0 mm, vias 11 -> 16
- net /DAC_CS: track 0.00 -> 31.3 mm, vias 0 -> 1
- net /DAC_SCK: track 0.00 -> 29.7 mm, vias 0 -> 1
- net /DAC_SDI: track 0.00 -> 26.4 mm, vias 0 -> 1
- net /LMX_MUXOUT: track 0.00 -> 24.6 mm, vias 0 -> 2
- net Net-(R207-Pad1): track 1.05 -> 20.3 mm, vias 1 -> 2
- net Net-(R205-Pad1): track 1.75 -> 18.9 mm, vias 1 -> 2
- net Net-(R206-Pad1): track 2.29 -> 19.2 mm, vias 1 -> 2
- net GND: track 168.0 -> 183.8 mm, vias 90 -> 109
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- added copper zone on F.Cu, net GND
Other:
- board text added: "PORT 1"
- board text added: "PORT 2"
- board text removed: "PORT 2 15 VDC MAX 20 dBm MAX PORT 1"
